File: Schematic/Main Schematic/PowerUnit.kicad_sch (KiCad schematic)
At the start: 20 parts, among them J6 USB_B_Micro

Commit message: I've added the local footprints and gerber files into the repo
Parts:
- BT?: footprint A_New_folder:18650_Holder_SMD -> Local_Footprints:18650_Holder_SMD
- C?: footprint A_New_folder:C1206 -> Local_Footprints:C1206
- IC?: footprint A_New_folder:SOT-23-6_L2.9-W1.6-P0.95-LS2.8-BR -> Local_Footprints:SOT-23-6_L2.9-W1.6-P0.95-LS2.8-BR
- J6: footprint A_New_folder:MICRO-USB-SMD_MICROXNJ -> Local_Footprints:MICRO-USB-SMD_MICROXNJ
- Q?: footprint A_New_folder:TSSOP-8_L4.4-W3.0-P0.65-LS6.4-BL-2 -> Local_Footprints:TSSOP-8_L4.4-W3.0-P0.65-LS6.4-BL-2
- R2, R?: footprint A_New_folder:R0402 -> Local_Footprints:R0402
- R?: footprint A_New_folder:R0603 -> Local_Footprints:C1206
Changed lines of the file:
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@@
       (effects (font (size 1.27 1.27)))
     )
-    (property "Footprint" "A_New_folder:TSSOP-8_L4.4-W3.0-P0.65-LS6.4-BL-2" (at 179.07 173.66 0)
+    (property "Footprint" "Local_Footprints:TSSOP-8_L4.4-W3.0-P0.65-LS6.4-BL-2" (at 179.07 173.66 0)
       (effects (font (size 1.27 1.27)) (justify left top) hide)
     )
@@
       (effects (font (size 1.27 1.27)))
     )
-    (property "Footprint" "A_New_folder:MICRO-USB-SMD_MICROXNJ" (at 34.036 74.93 0)
+    (property "Footprint" "Local_Footprints:MICRO-USB-SMD_MICROXNJ" (at 34.036 74.93 0)
       (effects (font (size 1.27 1.27)) hide)
     )
@@
       (effects (font (size 1.27 1.27)))
     )
-    (property "Footprint" "A_New_folder:R0603" (at 187.96 60.198 90)
+    (property "Footprint" "Local_Footprints:C1206" (at 187.96 60.198 90)
       (effects (font (size 1.27 1.27)) hide)
     )
@@
       (effects (font (size 1.27 1.27)))
     )
-    (property "Footprint" "A_New_folder:R0402" (at 146.558 71.12 90)
+    (property "Footprint" "Local_Footprints:R0402" (at 146.558 71.12 90)
       (effects (font (size 1.27 1.27)) hide)
     )
@@
       (effects (font (size 1.27 1.27)) (justify left))
     )
-    (property "Footprint" "A_New_folder:R0402" (at 97.282 73.66 90)
+    (property "Footprint" "Local_Footprints:R0402" (at 97.282 73.66 90)
       (effects (font (size 1.27 1.27)) hide)
     )
@@
       (effects (font (size 1.27 1.27)))
     )
-    (property "Footprint" "A_New_folder:SOT-23-6_L2.9-W1.6-P0.95-LS2.8-BR" (at 173.99 150.8 0)
+    (property "Footprint" "Local_Footprints:SOT-23-6_L2.9-W1.6-P0.95-LS2.8-BR" (at 173.99 150.8 0)
       (effects (font (size 1.27 1.27)) (justify left top) hide)
     )
@@
       (effects (font (size 1.27 1.27)) (justify left))
     )
-    (property "Footprint" "A_New_folder:C1206" (at 203.2 71.12 0)
+    (property "Footprint" "Local_Footprints:C1206" (at 203.2 71.12 0)
       (effects (font (size 1.27 1.27)) hide)
     )
@@
       (effects (font (size 1.27 1.27)) (justify left))
     )
-    (property "Footprint" "A_New_folder:18650_Holder_SMD" (at 251.46 72.136 90)
-      (effects (font (size 1.27 1.27)) hide)
-    )
+    (property "Footprint" "Local_Footprints:18650_Holder_SMD" (at 251.46 72.136 90)
+      (effects (font (size 1.27 1.27)) hide)
+    )

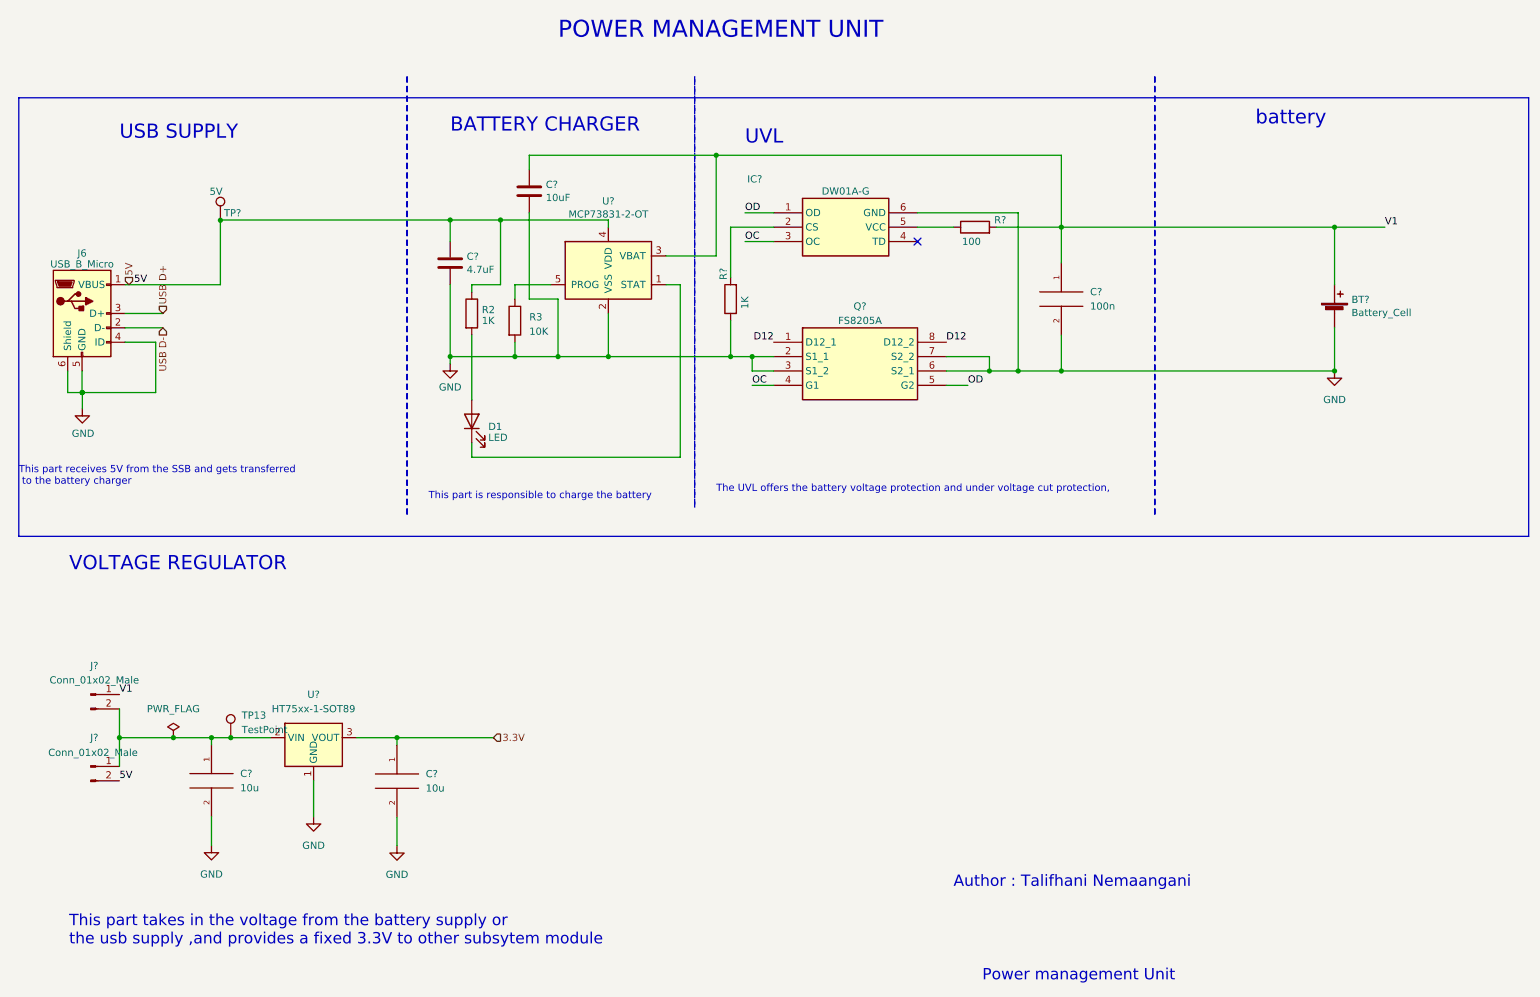
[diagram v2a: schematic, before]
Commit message: LED added for visuals
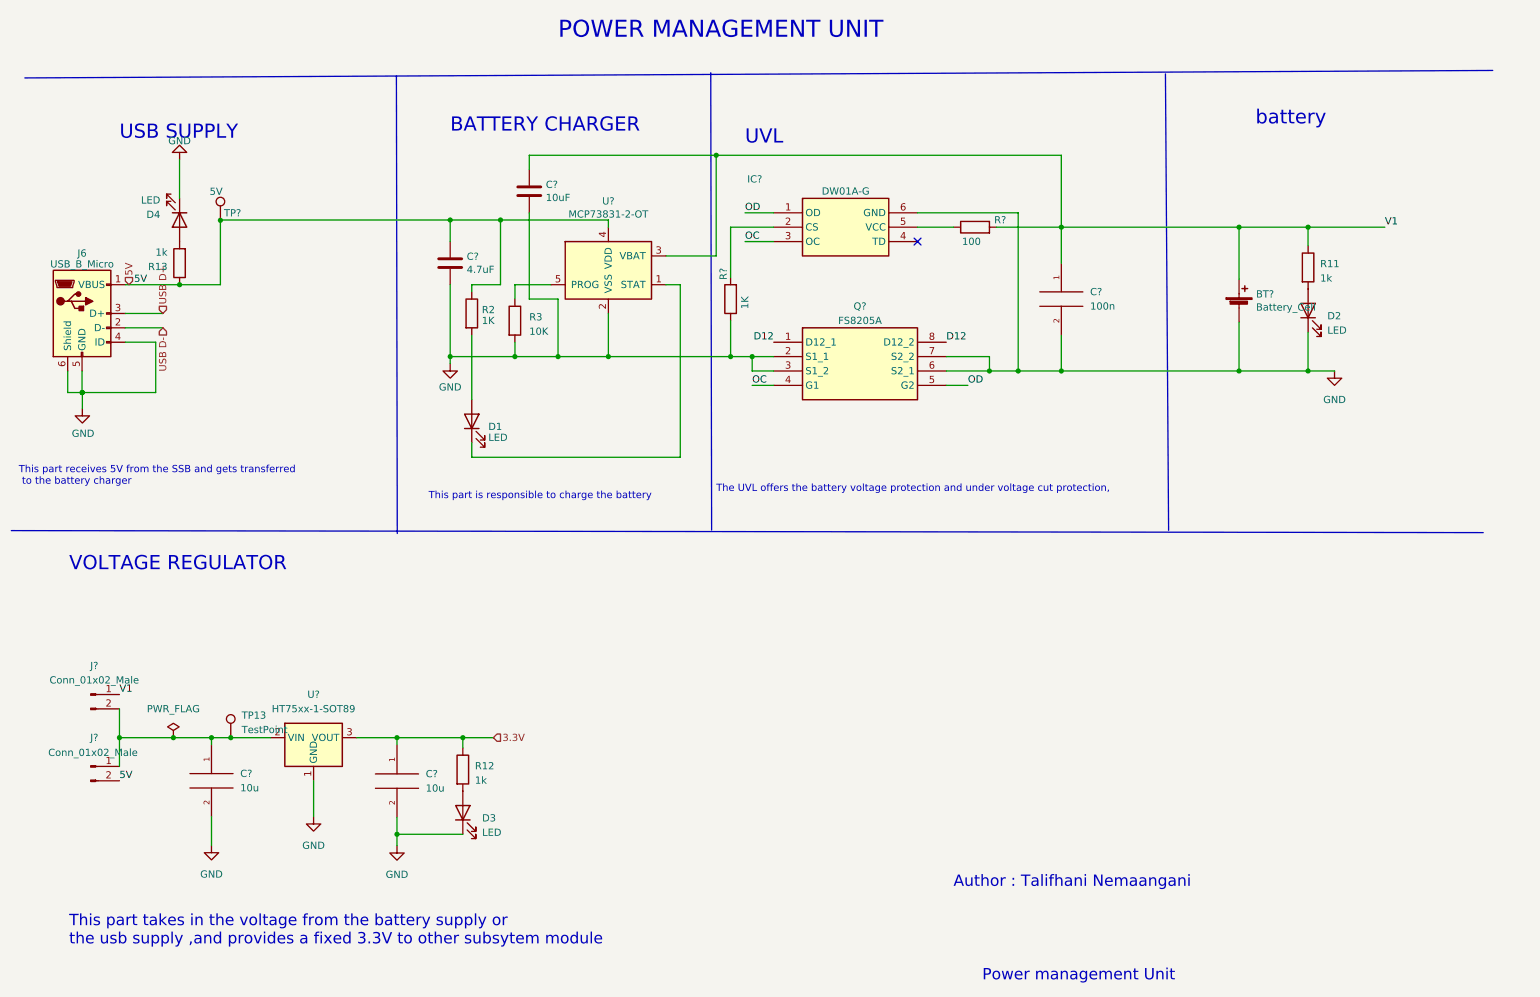
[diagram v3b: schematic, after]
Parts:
- added D2, D3, D4: LED, symbol Device:LED
- added R11, R12, R13: 1k, symbol Device:R
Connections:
- net 3.3V: now also R12.1
- net 5V: now also R13.1
- net GND: now also D2.1 (K), D3.1 (K), D4.1 (K)
- net V1: now also R11.1
- new net: D2.2 (A), R11.2
- new net: D3.2 (A), R12.2
- new net: D4.2 (A), R13.2
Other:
- moved on the sheet: BT?

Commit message: Added more led for visual indications, also changed debugger pins to 9 pins for 3.3v pin
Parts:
- D2, D3, D4: footprint (none) -> LED_THT:LED_D3.0mm
- R11, R12, R13: footprint (none) -> Local_Footprints:R0402
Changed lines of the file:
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@@
       (effects (font (size 1.27 1.27)) (justify left))
     )
-    (property "Footprint" "" (at 245.0084 65.532 90)
+    (property "Footprint" "Local_Footprints:R0402" (at 245.0084 65.532 90)
       (effects (font (size 1.27 1.27)) hide)
     )
@@
       (effects (font (size 1.27 1.27)) (justify right))
     )
-    (property "Footprint" "" (at 97.4852 161.8488 0)
+    (property "Footprint" "LED_THT:LED_D3.0mm" (at 97.4852 161.8488 0)
       (effects (font (size 1.27 1.27)) hide)
     )
@@
       (effects (font (size 1.27 1.27)) (justify left))
     )
-    (property "Footprint" "" (at 49.2252 64.77 90)
+    (property "Footprint" "Local_Footprints:R0402" (at 49.2252 64.77 90)
       (effects (font (size 1.27 1.27)) hide)
     )
@@
       (effects (font (size 1.27 1.27)) (justify right))
     )
-    (property "Footprint" "" (at 246.7864 73.152 0)
+    (property "Footprint" "LED_THT:LED_D3.0mm" (at 246.7864 73.152 0)
       (effects (font (size 1.27 1.27)) hide)
     )
@@
       (effects (font (size 1.27 1.27)) (justify right))
     )
-    (property "Footprint" "" (at 47.4472 57.15 0)
+    (property "Footprint" "LED_THT:LED_D3.0mm" (at 47.4472 57.15 0)
       (effects (font (size 1.27 1.27)) hide)
     )
@@
       (effects (font (size 1.27 1.27)) (justify left))
     )
-    (property "Footprint" "" (at 95.7072 154.2288 90)
-      (effects (font (size 1.27 1.27)) hide)
-    )
+    (property "Footprint" "Local_Footprints:R0402" (at 95.7072 154.2288 90)
+      (effects (font (size 1.27 1.27)) hide)
+    )

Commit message: Design done
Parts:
- removed D2: LED, LED_THT:LED_D3.0mm, symbol Device:LED
- removed R11: 1k, Local_Footprints:R0402, symbol Device:R
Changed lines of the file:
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@@
   (junction (at 95.25 81.28) (diameter 0) (color 0 0 0 0)
   )
-  (junction (at 246.7864 58.42) (diameter 0) (color 0 0 0 0)
-  )
   (junction (at 36.83 148.59) (diameter 0) (color 0 0 0 0)
   )
@@
   )
   (junction (at 47.4472 68.58) (diameter 0) (color 0 0 0 0)
-  )
-  (junction (at 246.7864 83.82) (diameter 0) (color 0 0 0 0)
   )
   (junction (at 234.5944 58.42) (diameter 0) (color 0 0 0 0)
@@
     (stroke (width 0) (type default))
   )
-  (wire (pts (xy 234.5944 58.42) (xy 246.7864 58.42))
-    (stroke (width 0) (type default))
-  )
   (wire (pts (xy 85.852 165.6588) (xy 85.852 167.6908))
     (stroke (width 0) (type default))
@@
     (stroke (width 0) (type default))
   )
-  (wire (pts (xy 246.7864 83.82) (xy 251.46 83.82))
+  (wire (pts (xy 234.5944 83.82) (xy 251.46 83.82))
     (stroke (width 0) (type default))
   )
@@
     (stroke (width 0) (type default))
   )
-  (wire (pts (xy 246.7864 58.42) (xy 246.7864 61.722))
-    (stroke (width 0) (type default))
-  )
   (wire (pts (xy 97.4852 148.59) (xy 97.4852 150.4188))
     (stroke (width 0) (type default))
@@
     (stroke (width 0) (type default))
   )
-  (wire (pts (xy 246.7864 76.962) (xy 246.7864 83.82))
-    (stroke (width 0) (type default))
-  )
   (wire (pts (xy 177.8 58.42) (xy 184.15 58.42))
     (stroke (width 0) (type default))
@@
     (stroke (width 0) (type default))
   )
-  (wire (pts (xy 234.5944 83.82) (xy 246.7864 83.82))
-    (stroke (width 0) (type default))
-  )
   (wire (pts (xy 36.83 148.59) (xy 46.355 148.59))
     (stroke (width 0) (type default))
@@
     (stroke (width 0) (type default))
   )
-  (wire (pts (xy 246.7864 58.42) (xy 260.35 58.42))
+  (wire (pts (xy 234.5944 58.42) (xy 260.35 58.42))
     (stroke (width 0) (type default))
   )
@@
         (path "/81c41bad-bb43-41af-b405-18d135a809b1/297def35-fe1a-4185-9e34-6248c2c818f7"
           (reference "#PWR02") (unit 1)
-        )
-      )
-    )
-  )
-  (symbol (lib_id "Device:R") (at 246.7864 65.532 0) (unit 1)
-    (in_bom yes) (on_board yes) (dnp no) (fields_autoplaced)
-    (property "Reference" "R11" (at 248.92 64.897 0)
-      (effects (font (size 1.27 1.27)) (justify left))
-    )
-    (property "Value" "1k" (at 248.92 67.437 0)
-      (effects (font (size 1.27 1.27)) (justify left))
-    )
-    (property "Footprint" "Local_Footprints:R0402" (at 245.0084 65.532 90)
-      (effects (font (size 1.27 1.27)) hide)
-    )
-    (property "Datasheet" "~" (at 246.7864 65.532 0)
-      (effects (font (size 1.27 1.27)) hide)
-    )
-    (pin "1")
-    (pin "2")
-    (instances
-      (project "Main Schematic"
-        (path "/81c41bad-bb43-41af-b405-18d135a809b1/297def35-fe1a-4185-9e34-6248c2c818f7"
-          (reference "R11") (unit 1)
         )
       )
@@
         )
       )
-    )
-  )
-  (symbol (lib_id "Device:LED") (at 246.7864 73.152 90) (unit 1)
-    (in_bom yes) (on_board yes) (dnp no) (fields_autoplaced)
-    (property "Reference" "D2" (at 250.19 74.1045 90)
-      (effects (font (size 1.27 1.27)) (justify right))
-    )
-    (property "Value" "LED" (at 250.19 76.6445 90)
-      (effects (font (size 1.27 1.27)) (justify right))
-    )
-    (property "Footprint" "LED_THT:LED_D3.0mm" (at 246.7864 73.152 0)
-      (effects (font (size 1.27 1.27)) hide)
-    )
-    (property "Datasheet" "~" (at 246.7864 73.152 0)
-      (effects (font (size 1.27 1.27)) hide)
-    )
-    (pin "1")
-    (pin "2")
-    (instances
-      (project "Main Schematic"
-        (path "/81c41bad-bb43-41af-b405-18d135a809b1/297def35-fe1a-4185-9e34-6248c2c818f7"
-          (reference "D2") (unit 1)
-        )
-      )

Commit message: Design part Done
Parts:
- C?: footprint Capacitor_SMD:C_0201_0603Metric -> Local_Footprints:C0805
- R12, R13, R2, R?: footprint Local_Footprints:R0402 -> Local_Footprints:R0805
- R3: footprint Resistor_SMD:R_1206_3216Metric -> Local_Footprints:R0805
- R?: footprint Local_Footprints:C1206 -> Local_Footprints:R0805
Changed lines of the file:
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@@
       (effects (font (size 1.27 1.27)))
     )
-    (property "Footprint" "Local_Footprints:C1206" (at 187.96 60.198 90)
+    (property "Footprint" "Local_Footprints:R0805" (at 187.96 60.198 90)
       (effects (font (size 1.27 1.27)) hide)
     )
@@
       (effects (font (size 1.27 1.27)))
     )
-    (property "Footprint" "Local_Footprints:R0402" (at 146.558 71.12 90)
+    (property "Footprint" "Local_Footprints:R0805" (at 146.558 71.12 90)
       (effects (font (size 1.27 1.27)) hide)
     )
@@
       (effects (font (size 1.27 1.27)) (justify left))
     )
-    (property "Footprint" "Local_Footprints:R0402" (at 49.2252 64.77 90)
+    (property "Footprint" "Local_Footprints:R0805" (at 49.2252 64.77 90)
       (effects (font (size 1.27 1.27)) hide)
     )
@@
       (effects (font (size 1.27 1.27)) (justify left))
     )
-    (property "Footprint" "Capacitor_SMD:C_0201_0603Metric" (at 96.2152 68.58 0)
+    (property "Footprint" "Local_Footprints:C0805" (at 96.2152 68.58 0)
       (effects (font (size 1.27 1.27)) hide)
     )
@@
       (effects (font (size 1.27 1.27)) (justify left))
     )
-    (property "Footprint" "Local_Footprints:R0402" (at 97.282 73.66 90)
+    (property "Footprint" "Local_Footprints:R0805" (at 97.282 73.66 90)
       (effects (font (size 1.27 1.27)) hide)
     )
@@
       (effects (font (size 1.27 1.27)) (justify left))
     )
-    (property "Footprint" "Resistor_SMD:R_1206_3216Metric" (at 104.902 74.93 90)
+    (property "Footprint" "Local_Footprints:R0805" (at 104.902 74.93 90)
       (effects (font (size 1.27 1.27)) hide)
     )
@@
       (effects (font (size 1.27 1.27)) (justify left))
     )
-    (property "Footprint" "Local_Footprints:R0402" (at 95.7072 154.2288 90)
-      (effects (font (size 1.27 1.27)) hide)
-    )
+    (property "Footprint" "Local_Footprints:R0805" (at 95.7072 154.2288 90)
+      (effects (font (size 1.27 1.27)) hide)
+    )

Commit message: edit
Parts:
- removed U?: HT75xx-1-SOT89, Package_TO_SOT_SMD:SOT-89-3, symbol Regulator_Linear:HT75xx-1-SOT89
- added U1: MCP1700x-330xxTT, Package_TO_SOT_SMD:SOT-23, symbol Regulator_Linear:MCP1700x-330xxTT
- C? (x2): value 10u -> 1uF
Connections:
- net 3.3V: now also U1.2 (VO)
- net GND: now also U1.1 (GND)
- net at C?.1, J?.1 (Pin_1), J?.2 (Pin_2)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: now also U1.3 (VI)
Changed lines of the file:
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@@
+    (stroke (width 0) (type default))
+  )
+  (wire (pts (xy 56.4896 148.59) (xy 63.5 148.59))
     (stroke (width 0) (type default))
   )
@@
   )
   (wire (pts (xy 99.06 77.47) (xy 99.06 88.9))
-    (stroke (width 0) (type default))
-  )
-  (wire (pts (xy 56.4896 148.59) (xy 63.5 148.59))
     (stroke (width 0) (type default))
   )
@@
   (symbol (lib_id "pspice:CAP") (at 53.086 156.21 0) (unit 1)
     (in_bom yes) (on_board yes) (dnp no) (fields_autoplaced)
-    (property "Reference" "C?" (at 58.166 154.9399 0)
-      (effects (font (size 1.27 1.27)) (justify left))
-    )
-    (property "Value" "10u" (at 58.166 157.4799 0)
+    (property "Reference" "C?" (at 58.42 155.575 0)
+      (effects (font (size 1.27 1.27)) (justify left))
+    )
+    (property "Value" "1uF" (at 58.42 158.115 0)
       (effects (font (size 1.27 1.27)) (justify left))
     )
@@
     )
   )
-  (symbol (lib_id "Regulator_Linear:HT75xx-1-SOT89") (at 71.12 151.13 0) (unit 1)
-    (in_bom yes) (on_board yes) (dnp no) (fields_autoplaced)
-    (property "Reference" "U?" (at 71.12 140.97 0)
-      (effects (font (size 1.27 1.27)))
-    )
-    (property "Value" "HT75xx-1-SOT89" (at 71.12 143.51 0)
-      (effects (font (size 1.27 1.27)))
-    )
-    (property "Footprint" "Package_TO_SOT_SMD:SOT-89-3" (at 71.12 142.875 0)
-      (effects (font (size 1.27 1.27) italic) hide)
-    )
-    (property "Datasheet" "https://www.holtek.com/documents/10179/116711/HT75xx-1v250.pdf" (at 71.12 148.59 0)
-      (effects (font (size 1.27 1.27)) hide)
-    )
-    (pin "1")
-    (pin "2")
-    (pin "3")
-    (instances
-      (project "power"
-        (path "/00318b70-98db-4150-aae9-0fe9db9b4f56"
-          (reference "U?") (unit 1)
-        )
-      )
-      (project "Main Schematic"
-        (path "/81c41bad-bb43-41af-b405-18d135a809b1/297def35-fe1a-4185-9e34-6248c2c818f7"
-          (reference "U1") (unit 1)
-        )
-      )
-    )
-  )
   (symbol (lib_id "Connector:USB_B_Micro") (at 30.226 73.66 0) (unit 1)
     (in_bom yes) (on_board yes) (dnp no) (fields_autoplaced)
@@
   (symbol (lib_id "pspice:CAP") (at 85.852 156.2608 0) (unit 1)
     (in_bom yes) (on_board yes) (dnp no) (fields_autoplaced)
-    (property "Reference" "C?" (at 90.932 154.9907 0)
-      (effects (font (size 1.27 1.27)) (justify left))
-    )
-    (property "Value" "10u" (at 90.932 157.5307 0)
+    (property "Reference" "C?" (at 91.44 155.6258 0)
+      (effects (font (size 1.27 1.27)) (justify left))
+    )
+    (property "Value" "1uF" (at 91.44 158.1658 0)
       (effects (font (size 1.27 1.27)) (justify left))
     )
@@
     )
   )
+  (symbol (lib_id "Regulator_Linear:MCP1700x-330xxTT") (at 71.12 148.59 0) (unit 1)
+    (in_bom yes) (on_board yes) (dnp no) (fields_autoplaced)
+    (property "Reference" "U1" (at 71.12 142.1892 0)
+      (effects (font (size 1.27 1.27)))
+    )
+    (property "Value" "MCP1700x-330xxTT" (at 71.12 144.7292 0)
+      (effects (font (size 1.27 1.27)))
+    )
+    (property "Footprint" "Package_TO_SOT_SMD:SOT-23" (at 71.12 142.875 0)
+      (effects (font (size 1.27 1.27)) hide)
+    )
+    (property "Datasheet" "http://ww1.microchip.com/downloads/en/DeviceDoc/20001826D.pdf" (at 71.12 148.59 0)
+      (effects (font (size 1.27 1.27)) hide)
+    )
+    (pin "1")
+    (pin "2")
+    (pin "3")
+    (instances
+      (project "Main Schematic"
+        (path "/81c41bad-bb43-41af-b405-18d135a809b1/297def35-fe1a-4185-9e34-6248c2c818f7"
+          (reference "U1") (unit 1)
+        )
+      )
+    )
+  )
   (symbol (lib_id "Device:Battery_Cell") (at 234.5944 72.6948 0) (unit 1)
     (in_bom yes) (on_board yes) (dnp no)
@@
   )
   (symbol (lib_id "Connector:TestPoint") (at 56.4896 148.59 0) (unit 1)
-    (in_bom yes) (on_board yes) (dnp no) (fields_autoplaced)
+    (in_bom yes) (on_board yes) (dnp no)
     (property "Reference" "TP13" (at 58.42 144.653 0)
       (effects (font (size 1.27 1.27)) (justify left))
     )
-    (property "Value" "TestPoint" (at 58.42 147.193 0)
-      (effects (font (size 1.27 1.27)) (justify left))
-    )
+    (property "Value" "TestPoint" (at 53.5686 150.241 0)
+      (effects (font (size 1.27 1.27)) (justify left))
+    )
